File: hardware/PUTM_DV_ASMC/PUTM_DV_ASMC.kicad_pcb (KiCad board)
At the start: 4 copper layers, 80 x 60 mm, 172 parts, among them IC1 BTS722204ESAXUMA1, IC2 BTS722204ESAXUMA1, J1 FTSH-107-01-L-D-K, J2 IPBS-110-01-XX-D-GP, Q1 30V/5A, T1 TP_VCC, T2 TP_+5V, T3 TP_+3V3, T4 TP_GND, T5 TP_GND, T6 TP_VCC, T7 TP_GND, T8 TP_+5V, T9 TP_GND, U1 LM4040C33FTA, U2 STM32G484RETx, U3 LM1117-3.3, U4 TPS54202HDDCR, U5 ADM3057ExRW, U6 ADM3057ExRW, U8 TLP291-4, Y1 ATX-11-F-32.000MHZ-F05-T

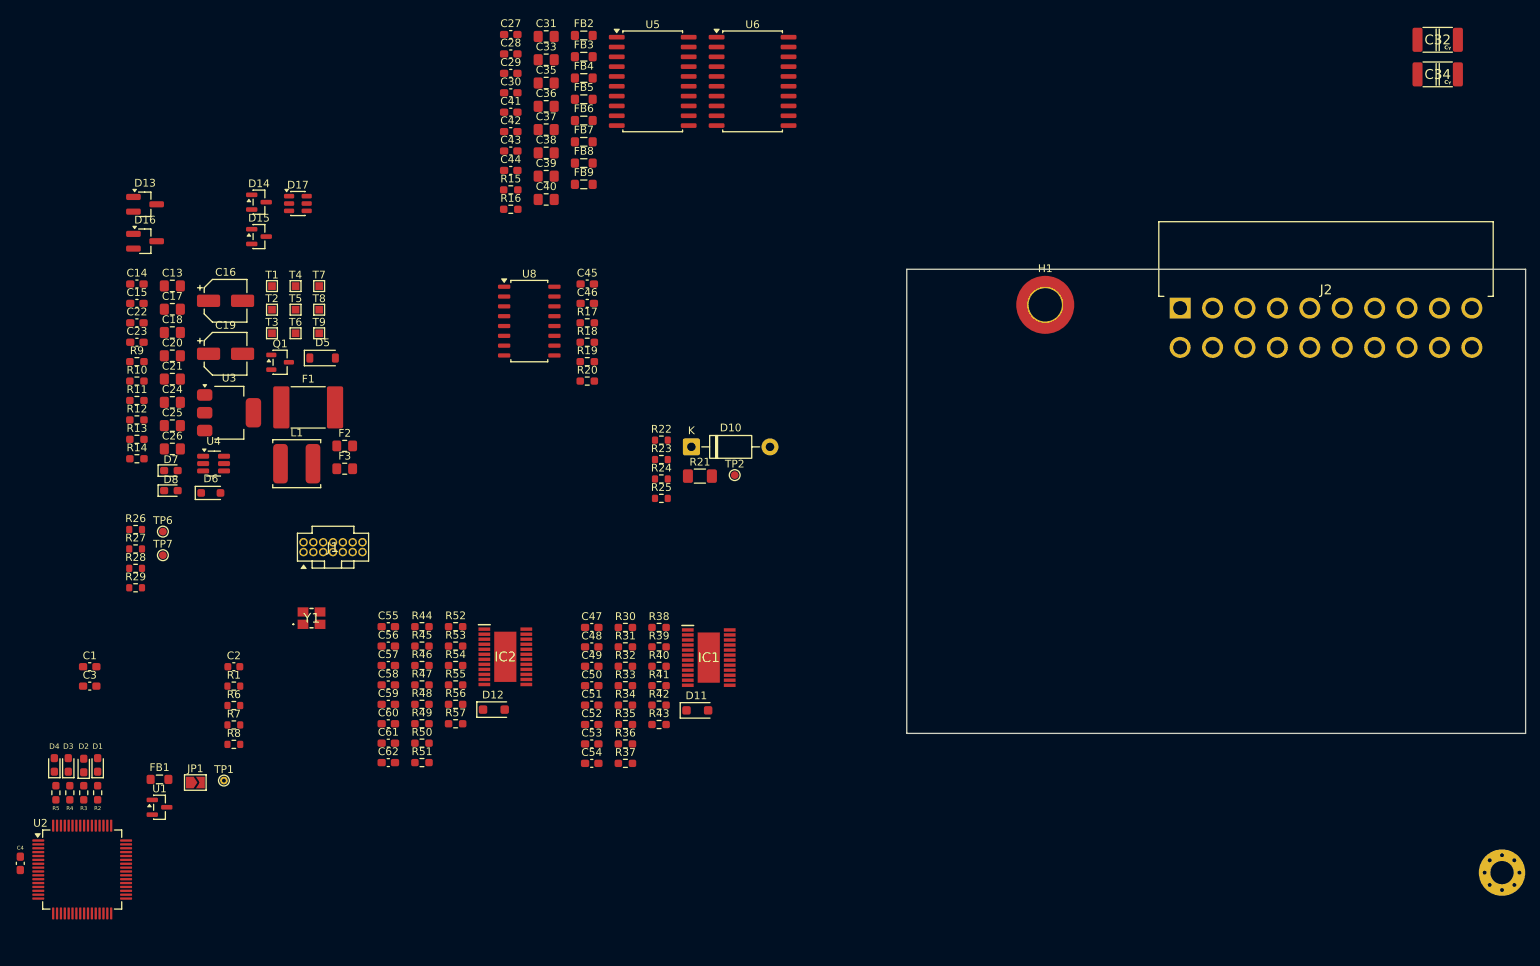
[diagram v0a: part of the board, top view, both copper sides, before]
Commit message: tylko dwa bledy z can - schemat na wykonczeniu
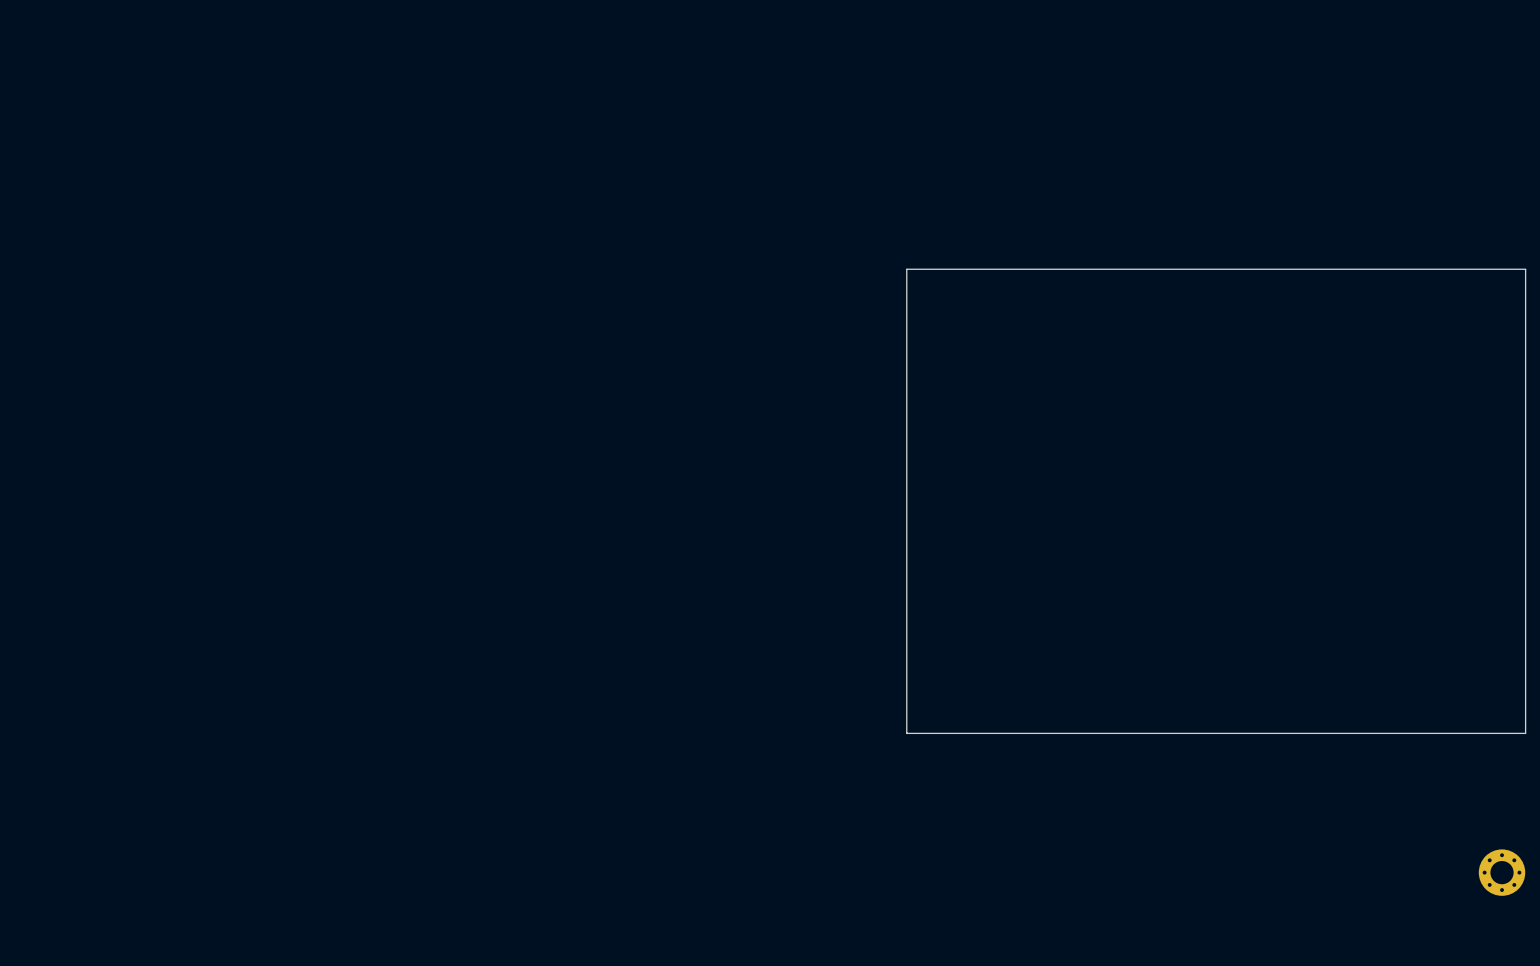
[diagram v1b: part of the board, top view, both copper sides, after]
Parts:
- removed C1, C3: 100nF, Capacitor_SMD:C_0603_1608Metric_Pad1.08x0.95mm_HandSolder
- removed C13, C18, C20: 10u, Capacitor_SMD:C_0805_2012Metric_Pad1.18x1.45mm_HandSolder
- removed C14, C15, C22, C23, C27, C28, C41, C43, C45, C46, C48, C56: 100n, Capacitor_SMD:C_0603_1608Metric_Pad1.08x0.95mm_HandSolder
- removed C16, C19: 22u, Capacitor_SMD:CP_Elec_5x5.8
- removed C17, C21, C24, C25, C26: 22u, Capacitor_SMD:C_0805_2012Metric_Pad1.18x1.45mm_HandSolder
- removed C2: 100n, Capacitor_SMD:C_0603_1608Metric
- removed C29, C30, C42, C44, C51, C52, C53, C54, C59, C60, C61, C62: 10n, Capacitor_SMD:C_0603_1608Metric_Pad1.08x0.95mm_HandSolder
- removed C31, C33, C35, C36, C37, C38, C39, C40: 47u, Capacitor_SMD:C_0805_2012Metric_Pad1.18x1.45mm_HandSolder
- removed C32, C34: 4.7nF/Y2, CAPC5728X280N:CAPC5728X280N
- removed C4: 6p, Capacitor_SMD:C_0603_1608Metric_Pad1.08x0.95mm_HandSolder
- removed C47, C55: 220p, Capacitor_SMD:C_0603_1608Metric_Pad1.08x0.95mm_HandSolder
- removed C49, C57: 22n, Capacitor_SMD:C_0603_1608Metric_Pad1.08x0.95mm_HandSolder
- removed C50, C58: 470n, Capacitor_SMD:C_0603_1608Metric_Pad1.08x0.95mm_HandSolder
- removed D1, D2, D3, D4: LED, LED_SMD:LED_0603_1608Metric_Pad1.05x0.95mm_HandSolder
- removed D10: 1N4007, Diode_THT:D_DO-41_SOD81_P10.16mm_Horizontal
- removed D11, D12: 40V/3A, Diode_SMD:D_SOD-123F
- removed D13, D16: PESD5V0L2BT, Package_TO_SOT_SMD:SOT-23_Handsoldering
- removed D14: BZX84C5V6, Package_TO_SOT_SMD:SOT-23
- removed D15: BZX84C3V6-E3-08, Package_TO_SOT_SMD:SOT-23
- removed D17: 3.6V/400W, Package_TO_SOT_SMD:SOT-23-6
- removed D5: 30V/200W, Diode_SMD:D_SOD-123
- removed D6: 9V1/200mW, Diode_SMD:D_SOD-323_HandSoldering
- removed D7: LED_+3V3, LED_SMD:LED_0603_1608Metric_Pad1.05x0.95mm_HandSolder
- removed D8: LED_+5V, LED_SMD:LED_0603_1608Metric_Pad1.05x0.95mm_HandSolder
- removed F1: 33V/1A5, Fuse:Fuse_2920_7451Metric_Pad2.10x5.45mm_HandSolder
- removed F2, F3: 6V/1A, Fuse:Fuse_0805_2012Metric_Pad1.15x1.40mm_HandSolder
- removed FB1, FB2, FB3, FB4, FB5, FB6, FB7, FB8, FB9: 2K@100MHz, Inductor_SMD:L_0805_2012Metric_Pad1.05x1.20mm_HandSolder
- removed H1: MountingHole_Pad_MP, MountingHole:MountingHole_4.3mm_M4_DIN965_Pad_TopOnly
- removed IC1, IC2: BTS722204ESAXUMA1, PDM:SOP65P600X115-25N
- removed J1: FTSH-107-01-L-D-K, FTSH-107-XX-YYY-D-K:FTSH-107-XX-YYY-D-K
- removed J2: IPBS-110-01-XX-D-GP, PDM:IPBT110H1TDRAGP
- removed JP1: Jumper_2_Small_Bridged, Jumper:SolderJumper-2_P1.3mm_Open_TrianglePad1.0x1.5mm
- removed L1: 68u/1A4, Inductor_SMD:L_TDK_VLS6045EX_VLS6045AF
- removed Q1: 30V/5A, Package_TO_SOT_SMD:SOT-23-3
- removed R1: 1k, Resistor_SMD:R_0603_1608Metric
- removed R10, R14: 1k, Resistor_SMD:R_0603_1608Metric_Pad0.98x0.95mm_HandSolder
- removed R11: 510k, Resistor_SMD:R_0603_1608Metric_Pad0.98x0.95mm_HandSolder
- removed R12: 13k3, Resistor_SMD:R_0603_1608Metric_Pad0.98x0.95mm_HandSolder
- removed R13, R9: 100k, Resistor_SMD:R_0603_1608Metric_Pad0.98x0.95mm_HandSolder
- removed R15, R16: 100K, Resistor_SMD:R_0603_1608Metric_Pad0.98x0.95mm_HandSolder
- removed R17, R18: 2k, Resistor_SMD:R_0603_1608Metric_Pad0.98x0.95mm_HandSolder
- removed R19, R20, R38, R39, R40, R41, R52, R53, R54, R55: 10k, Resistor_SMD:R_0603_1608Metric_Pad0.98x0.95mm_HandSolder
- removed R2, R3, R4, R5: 1K, Resistor_SMD:R_0603_1608Metric_Pad0.98x0.95mm_HandSolder
- removed R21: 2.2k, Resistor_SMD:R_1206_3216Metric_Pad1.30x1.75mm_HandSolder
- removed R22, R23, R26, R28: 100R, Resistor_SMD:R_0603_1608Metric
- removed R24, R25, R27, R29, R6, R7, R8: 10k, Resistor_SMD:R_0603_1608Metric
- removed R30, R31, R32, R44, R45, R46: 4k7, Resistor_SMD:R_0603_1608Metric_Pad0.98x0.95mm_HandSolder
- removed R33, R47: 470R, Resistor_SMD:R_0603_1608Metric_Pad0.98x0.95mm_HandSolder
- removed R34, R35, R36, R37, R48, R49, R50, R51: 330R, Resistor_SMD:R_0603_1608Metric_Pad0.98x0.95mm_HandSolder
- removed R42, R56: 1k2, Resistor_SMD:R_0603_1608Metric_Pad0.98x0.95mm_HandSolder
- removed R43, R57: 47R, Resistor_SMD:R_0603_1608Metric_Pad0.98x0.95mm_HandSolder
- removed T1, T6: TP_VCC, TestPoint:TestPoint_Pad_1.0x1.0mm
- removed T2, T8: TP_+5V, TestPoint:TestPoint_Pad_1.0x1.0mm
- removed T3: TP_+3V3, TestPoint:TestPoint_Pad_1.0x1.0mm
- removed T4, T5, T7, T9: TP_GND, TestPoint:TestPoint_Pad_1.0x1.0mm
- removed TP1: TestPoint_Small, TestPoint:TestPoint_THTPad_D1.0mm_Drill0.5mm
- removed TP2, TP6, TP7: TestPoint_Small, TestPoint:TestPoint_Pad_D1.0mm
- removed U1: LM4040C33FTA, Package_TO_SOT_SMD:SOT-23
- removed U2: STM32G484RETx, Package_QFP:LQFP-64_10x10mm_P0.5mm
- removed U3: LM1117-3.3, Package_TO_SOT_SMD:SOT-223-3_TabPin2
- removed U4: TPS54202HDDCR, Package_TO_SOT_SMD:SOT-23-6_Handsoldering
- removed U5, U6: ADM3057ExRW, Package_SO:SOIC-20W_7.5x12.8mm_P1.27mm
- removed U8: TLP291-4, Package_SO:SOIC-16_4.55x10.3mm_P1.27mm
- removed Y1: ATX-11-F-32.000MHZ-F05-T, ATX11F32000MHZF05T:ATX11F32000MHZF05T

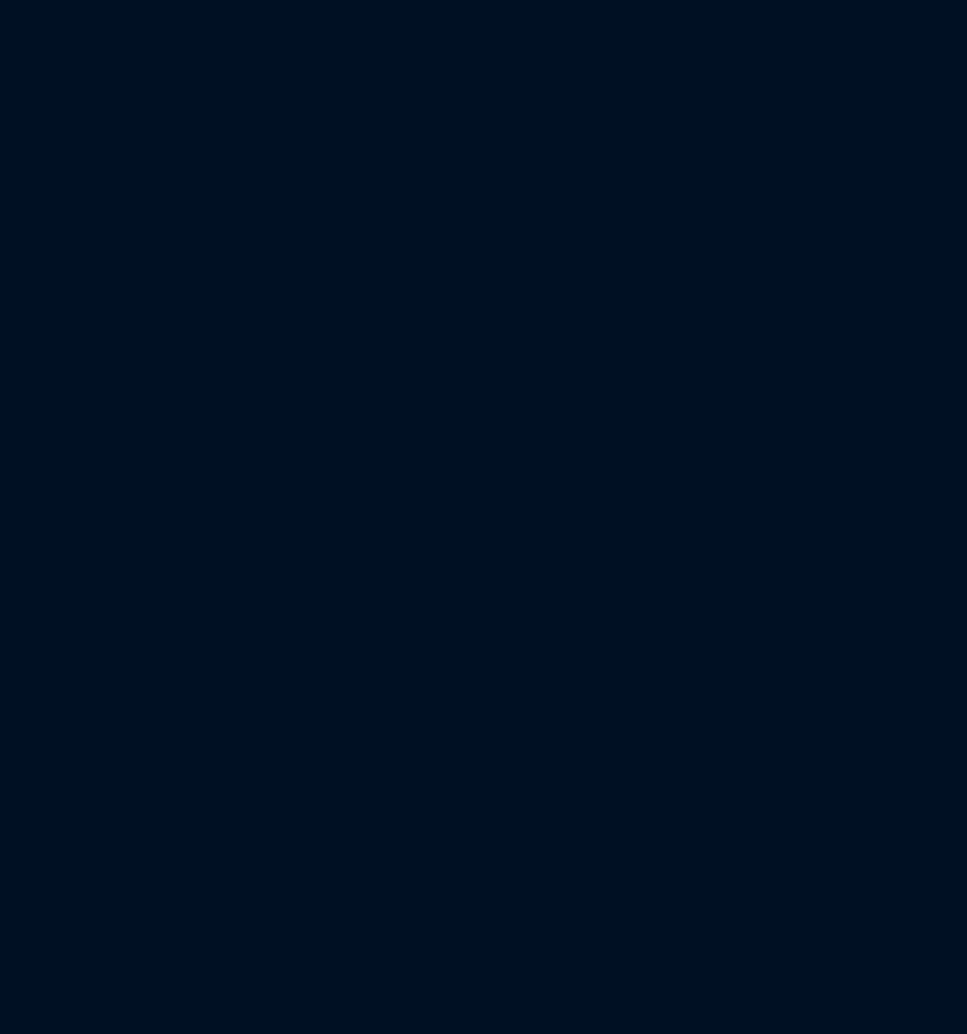
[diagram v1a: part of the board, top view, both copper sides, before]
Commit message: poprawki footprint
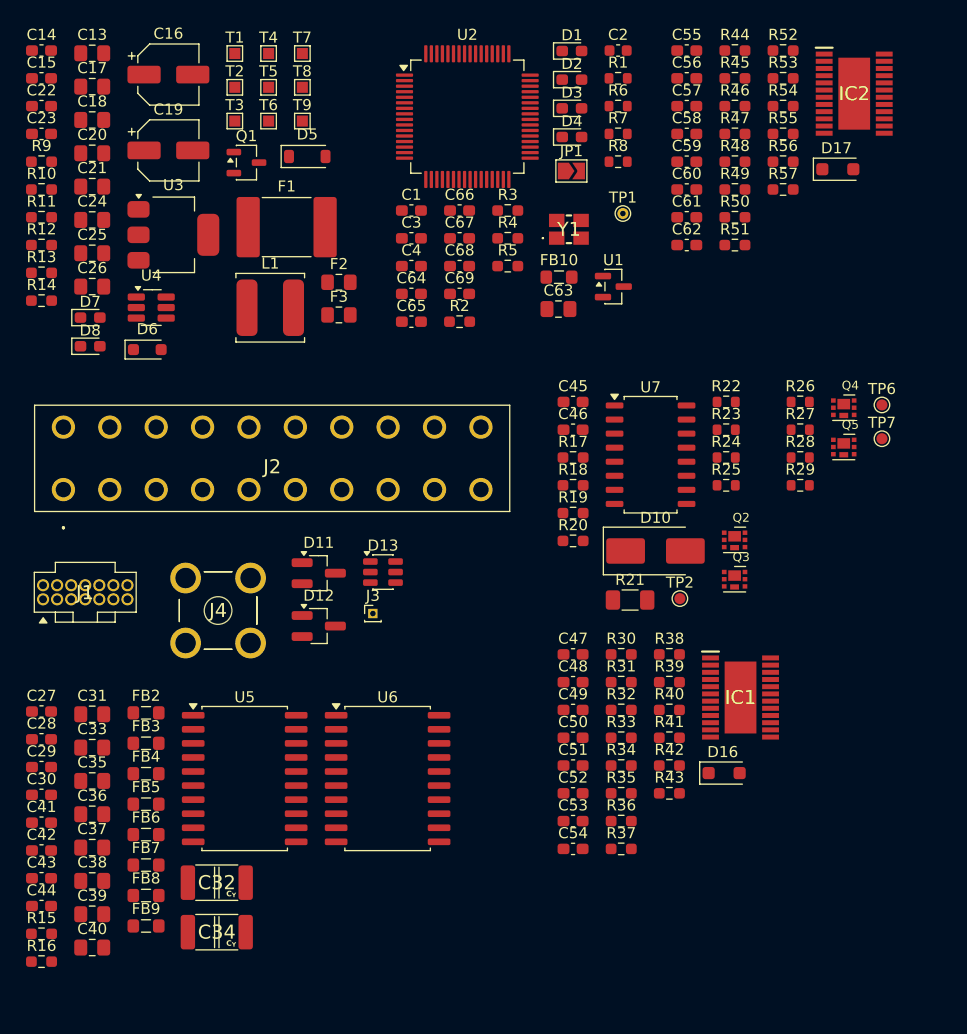
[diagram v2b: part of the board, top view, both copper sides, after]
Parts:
- added C1: 100nF, Capacitor_SMD:C_0603_1608Metric_Pad1.08x0.95mm_HandSolder, F.Cu at (27.1, 17.6)
- added C13: 10u, Capacitor_SMD:C_0805_2012Metric_Pad1.18x1.45mm_HandSolder, F.Cu at (-1.75, 3.40)
- added C14: 100n, Capacitor_SMD:C_0603_1608Metric_Pad1.08x0.95mm_HandSolder, F.Cu at (-6.33, 3.15)
- added C15: 100n, Capacitor_SMD:C_0603_1608Metric_Pad1.08x0.95mm_HandSolder, F.Cu at (-6.33, 5.67)
- added C16: 22u, Capacitor_SMD:CP_Elec_5x5.8, F.Cu at (5.13, 5.33)
- added C17: 22u, Capacitor_SMD:C_0805_2012Metric_Pad1.18x1.45mm_HandSolder, F.Cu at (-1.75, 6.42)
- added C18: 10u, Capacitor_SMD:C_0805_2012Metric_Pad1.18x1.45mm_HandSolder, F.Cu at (-1.75, 9.43)
- added C19: 22u, Capacitor_SMD:CP_Elec_5x5.8, F.Cu at (5.13, 12.2)
- added C2: 100n, Capacitor_SMD:C_0603_1608Metric, F.Cu at (45.8, 3.15)
- added C20: 10u, Capacitor_SMD:C_0805_2012Metric_Pad1.18x1.45mm_HandSolder, F.Cu at (-1.75, 12.4)
- added C21: 22u, Capacitor_SMD:C_0805_2012Metric_Pad1.18x1.45mm_HandSolder, F.Cu at (-1.75, 15.4)
- added C22: 100n, Capacitor_SMD:C_0603_1608Metric_Pad1.08x0.95mm_HandSolder, F.Cu at (-6.33, 8.18)
- added C23: 100n, Capacitor_SMD:C_0603_1608Metric_Pad1.08x0.95mm_HandSolder, F.Cu at (-6.33, 10.7)
- added C24: 22u, Capacitor_SMD:C_0805_2012Metric_Pad1.18x1.45mm_HandSolder, F.Cu at (-1.75, 18.5)
- added C25: 22u, Capacitor_SMD:C_0805_2012Metric_Pad1.18x1.45mm_HandSolder, F.Cu at (-1.75, 21.5)
- added C26: 22u, Capacitor_SMD:C_0805_2012Metric_Pad1.18x1.45mm_HandSolder, F.Cu at (-1.75, 24.5)
- added C27: 100n, Capacitor_SMD:C_0603_1608Metric_Pad1.08x0.95mm_HandSolder, F.Cu at (-6.33, 62.9)
- added C28: 100n, Capacitor_SMD:C_0603_1608Metric_Pad1.08x0.95mm_HandSolder, F.Cu at (-6.33, 65.4)
- added C29: 10n, Capacitor_SMD:C_0603_1608Metric_Pad1.08x0.95mm_HandSolder, F.Cu at (-6.33, 67.9)
- added C3: 100nF, Capacitor_SMD:C_0603_1608Metric_Pad1.08x0.95mm_HandSolder, F.Cu at (27.1, 20.1)
- added C30: 10n, Capacitor_SMD:C_0603_1608Metric_Pad1.08x0.95mm_HandSolder, F.Cu at (-6.33, 70.4)
- added C31: 47u, Capacitor_SMD:C_0805_2012Metric_Pad1.18x1.45mm_HandSolder, F.Cu at (-1.75, 63.1)
- added C32: 4.7nF/Y2, CAPC5728X280N:CAPC5728X280N, F.Cu at (9.51, 78.3)
- added C33: 47u, Capacitor_SMD:C_0805_2012Metric_Pad1.18x1.45mm_HandSolder, F.Cu at (-1.75, 66.1)
- added C34: 4.7nF/Y2, CAPC5728X280N:CAPC5728X280N, F.Cu at (9.51, 82.8)
- added C35: 47u, Capacitor_SMD:C_0805_2012Metric_Pad1.18x1.45mm_HandSolder, F.Cu at (-1.75, 69.1)
- added C36: 47u, Capacitor_SMD:C_0805_2012Metric_Pad1.18x1.45mm_HandSolder, F.Cu at (-1.75, 72.1)
- added C37: 47u, Capacitor_SMD:C_0805_2012Metric_Pad1.18x1.45mm_HandSolder, F.Cu at (-1.75, 75.1)
- added C38: 47u, Capacitor_SMD:C_0805_2012Metric_Pad1.18x1.45mm_HandSolder, F.Cu at (-1.75, 78.2)
- added C39: 47u, Capacitor_SMD:C_0805_2012Metric_Pad1.18x1.45mm_HandSolder, F.Cu at (-1.75, 81.2)
- added C4: 6p, Capacitor_SMD:C_0603_1608Metric_Pad1.08x0.95mm_HandSolder, F.Cu at (27.1, 22.6)
- added C40: 47u, Capacitor_SMD:C_0805_2012Metric_Pad1.18x1.45mm_HandSolder, F.Cu at (-1.75, 84.2)
- added C41: 100n, Capacitor_SMD:C_0603_1608Metric_Pad1.08x0.95mm_HandSolder, F.Cu at (-6.33, 72.9)
- added C42: 10n, Capacitor_SMD:C_0603_1608Metric_Pad1.08x0.95mm_HandSolder, F.Cu at (-6.33, 75.4)
- added C43: 100n, Capacitor_SMD:C_0603_1608Metric_Pad1.08x0.95mm_HandSolder, F.Cu at (-6.33, 77.9)
- added C44: 10n, Capacitor_SMD:C_0603_1608Metric_Pad1.08x0.95mm_HandSolder, F.Cu at (-6.33, 80.4)
- added C45: 100n, Capacitor_SMD:C_0603_1608Metric_Pad1.08x0.95mm_HandSolder, F.Cu at (41.7, 34.9)
- added C46: 100n, Capacitor_SMD:C_0603_1608Metric_Pad1.08x0.95mm_HandSolder, F.Cu at (41.7, 37.4)
- added C47: 220p, Capacitor_SMD:C_0603_1608Metric_Pad1.08x0.95mm_HandSolder, F.Cu at (41.7, 57.7)
- added C48: 100n, Capacitor_SMD:C_0603_1608Metric_Pad1.08x0.95mm_HandSolder, F.Cu at (41.7, 60.2)
- added C49: 22n, Capacitor_SMD:C_0603_1608Metric_Pad1.08x0.95mm_HandSolder, F.Cu at (41.7, 62.7)
- added C50: 470n, Capacitor_SMD:C_0603_1608Metric_Pad1.08x0.95mm_HandSolder, F.Cu at (41.7, 65.2)
- added C51: 10n, Capacitor_SMD:C_0603_1608Metric_Pad1.08x0.95mm_HandSolder, F.Cu at (41.7, 67.7)
- added C52: 10n, Capacitor_SMD:C_0603_1608Metric_Pad1.08x0.95mm_HandSolder, F.Cu at (41.7, 70.2)
- added C53: 10n, Capacitor_SMD:C_0603_1608Metric_Pad1.08x0.95mm_HandSolder, F.Cu at (41.7, 72.8)
- added C54: 10n, Capacitor_SMD:C_0603_1608Metric_Pad1.08x0.95mm_HandSolder, F.Cu at (41.7, 75.3)
- added C55: 220p, Capacitor_SMD:C_0603_1608Metric_Pad1.08x0.95mm_HandSolder, F.Cu at (52.0, 3.15)
- added C56: 100n, Capacitor_SMD:C_0603_1608Metric_Pad1.08x0.95mm_HandSolder, F.Cu at (52.0, 5.67)
- added C57: 22n, Capacitor_SMD:C_0603_1608Metric_Pad1.08x0.95mm_HandSolder, F.Cu at (52.0, 8.18)
- added C58: 470n, Capacitor_SMD:C_0603_1608Metric_Pad1.08x0.95mm_HandSolder, F.Cu at (52.0, 10.7)
- added C59: 10n, Capacitor_SMD:C_0603_1608Metric_Pad1.08x0.95mm_HandSolder, F.Cu at (52.0, 13.2)
- added C60: 10n, Capacitor_SMD:C_0603_1608Metric_Pad1.08x0.95mm_HandSolder, F.Cu at (52.0, 15.7)
- added C61: 10n, Capacitor_SMD:C_0603_1608Metric_Pad1.08x0.95mm_HandSolder, F.Cu at (52.0, 18.2)
- added C62: 10n, Capacitor_SMD:C_0603_1608Metric_Pad1.08x0.95mm_HandSolder, F.Cu at (52.0, 20.7)
- added C63: 10u, Capacitor_SMD:C_0805_2012Metric_Pad1.18x1.45mm_HandSolder, F.Cu at (40.4, 26.5)
- added C64: 100nF, Capacitor_SMD:C_0603_1608Metric_Pad1.08x0.95mm_HandSolder, F.Cu at (27.1, 25.1)
- added C65: 100nF, Capacitor_SMD:C_0603_1608Metric_Pad1.08x0.95mm_HandSolder, F.Cu at (27.1, 27.6)
- added C66: 100nF, Capacitor_SMD:C_0603_1608Metric_Pad1.08x0.95mm_HandSolder, F.Cu at (31.4, 17.6)
- added C67: 100nF, Capacitor_SMD:C_0603_1608Metric_Pad1.08x0.95mm_HandSolder, F.Cu at (31.4, 20.1)
- added C68: 100nF, Capacitor_SMD:C_0603_1608Metric_Pad1.08x0.95mm_HandSolder, F.Cu at (31.4, 22.6)
- added C69: 100nF, Capacitor_SMD:C_0603_1608Metric_Pad1.08x0.95mm_HandSolder, F.Cu at (31.4, 25.1)
- added D1: LED, LED_SMD:LED_0603_1608Metric_Pad1.05x0.95mm_HandSolder, F.Cu at (41.6, 3.19)
- added D10: SMBJ30A, Diode_SMD:D_SMB_Handsoldering, F.Cu at (49.1, 48.4)
- added D11: PESD5V0L2BT, Package_TO_SOT_SMD:SOT-23_Handsoldering, F.Cu at (18.7, 50.4)
- added D12: PESD5V0L2BT, Package_TO_SOT_SMD:SOT-23_Handsoldering, F.Cu at (18.7, 55.1)
- added D13: 3.6V/400W, Package_TO_SOT_SMD:SOT-23-6, F.Cu at (24.5, 50.3)
- added D16: 40V/3A, Diode_SMD:D_SOD-123F, F.Cu at (55.3, 68.4)
- added D17: 40V/3A, Diode_SMD:D_SOD-123F, F.Cu at (65.6, 13.9)
- added D2: LED, LED_SMD:LED_0603_1608Metric_Pad1.05x0.95mm_HandSolder, F.Cu at (41.6, 5.79)
- added D3: LED, LED_SMD:LED_0603_1608Metric_Pad1.05x0.95mm_HandSolder, F.Cu at (41.6, 8.38)
- added D4: LED, LED_SMD:LED_0603_1608Metric_Pad1.05x0.95mm_HandSolder, F.Cu at (41.6, 11.0)
- added D5: 30V/200W, Diode_SMD:D_SOD-123, F.Cu at (17.7, 12.7)
- added D6: 9V1/200mW, Diode_SMD:D_SOD-323_HandSoldering, F.Cu at (3.23, 30.2)
- added D7: LED_+3V3, LED_SMD:LED_0603_1608Metric_Pad1.05x0.95mm_HandSolder, F.Cu at (-1.93, 27.3)
- added D8: LED_+5V, LED_SMD:LED_0603_1608Metric_Pad1.05x0.95mm_HandSolder, F.Cu at (-1.93, 29.9)
- added F1: 33V/1A5, Fuse:Fuse_2920_7451Metric_Pad2.10x5.45mm_HandSolder, F.Cu at (15.8, 19.1)
- added F2: 6V/1A, Fuse:Fuse_0805_2012Metric_Pad1.15x1.40mm_HandSolder, F.Cu at (20.5, 24.1)
- added F3: 6V/1A, Fuse:Fuse_0805_2012Metric_Pad1.15x1.40mm_HandSolder, F.Cu at (20.5, 27.0)
- added FB10: 2K@100MHz, Inductor_SMD:L_0805_2012Metric_Pad1.05x1.20mm_HandSolder, F.Cu at (40.4, 23.6)
- added FB2: 2K@100MHz, Inductor_SMD:L_0805_2012Metric_Pad1.05x1.20mm_HandSolder, F.Cu at (3.12, 63.0)
- added FB3: 2K@100MHz, Inductor_SMD:L_0805_2012Metric_Pad1.05x1.20mm_HandSolder, F.Cu at (3.12, 65.7)
- added FB4: 2K@100MHz, Inductor_SMD:L_0805_2012Metric_Pad1.05x1.20mm_HandSolder, F.Cu at (3.12, 68.5)
- added FB5: 2K@100MHz, Inductor_SMD:L_0805_2012Metric_Pad1.05x1.20mm_HandSolder, F.Cu at (3.12, 71.2)
- added FB6: 2K@100MHz, Inductor_SMD:L_0805_2012Metric_Pad1.05x1.20mm_HandSolder, F.Cu at (3.12, 74.0)
- added FB7: 2K@100MHz, Inductor_SMD:L_0805_2012Metric_Pad1.05x1.20mm_HandSolder, F.Cu at (3.12, 76.7)
- added FB8: 2K@100MHz, Inductor_SMD:L_0805_2012Metric_Pad1.05x1.20mm_HandSolder, F.Cu at (3.12, 79.5)
- added FB9: 2K@100MHz, Inductor_SMD:L_0805_2012Metric_Pad1.05x1.20mm_HandSolder, F.Cu at (3.12, 82.2)
- added IC1: BTS722204ESAXUMA1, BTS722204ESAXUMA1:SOP65P600X115-25N, F.Cu at (56.8, 61.6)
- added IC2: BTS722204ESAXUMA1, BTS722204ESAXUMA1:SOP65P600X115-25N, F.Cu at (67.1, 7.05)
- added J1: FTSH-107-01-L-D-K, FTSH-107-XX-YYY-D-K:FTSH-107-XX-YYY-D-K, F.Cu at (-2.38, 52.1)
- added J2: IPBS-110-01-XX-D-GP, IPBS-110-01-T-D-GP:IPBS11001TDGP, F.Cu at (-4.35, 42.8)
- added J3: Conn_01x01_Socket, Connector_PinHeader_1.00mm:PinHeader_1x01_P1.00mm_Vertical, F.Cu at (23.6, 54.0)
- added J4: 74650073R, 74650073R:74650073R, F.Cu at (6.69, 56.7)
- added JP1: Jumper_2_Small_Bridged, Jumper:SolderJumper-2_P1.3mm_Open_TrianglePad1.0x1.5mm, F.Cu at (41.5, 14.0)
- added L1: 68u/1A4, Inductor_SMD:L_TDK_VLS6045EX_VLS6045AF, F.Cu at (14.3, 26.4)
- added Q1: 30V/5A, Package_TO_SOT_SMD:SOT-23-3, F.Cu at (12.2, 13.3)
- added Q2: BUK6D210, UDFN2020-6:Diodes_UDFN2020-6_Type-F, F.Cu at (56.3, 47.4)
- added Q3: BUK6D210, UDFN2020-6:Diodes_UDFN2020-6_Type-F, F.Cu at (56.3, 50.9)
- added Q4: BUK6D210, UDFN2020-6:Diodes_UDFN2020-6_Type-F, F.Cu at (66.1, 35.4)
- added Q5: BUK6D210, UDFN2020-6:Diodes_UDFN2020-6_Type-F, F.Cu at (66.1, 39.0)
- added R1: 1k, Resistor_SMD:R_0603_1608Metric, F.Cu at (45.8, 5.67)
- added R10: 1k, Resistor_SMD:R_0603_1608Metric_Pad0.98x0.95mm_HandSolder, F.Cu at (-6.33, 15.7)
- added R11: 510k, Resistor_SMD:R_0603_1608Metric_Pad0.98x0.95mm_HandSolder, F.Cu at (-6.33, 18.2)
- added R12: 13k3, Resistor_SMD:R_0603_1608Metric_Pad0.98x0.95mm_HandSolder, F.Cu at (-6.33, 20.7)
- added R13: 100k, Resistor_SMD:R_0603_1608Metric_Pad0.98x0.95mm_HandSolder, F.Cu at (-6.33, 23.2)
- added R14: 1k, Resistor_SMD:R_0603_1608Metric_Pad0.98x0.95mm_HandSolder, F.Cu at (-6.33, 25.7)
- added R15: 100K, Resistor_SMD:R_0603_1608Metric_Pad0.98x0.95mm_HandSolder, F.Cu at (-6.33, 82.9)
- added R16: 100K, Resistor_SMD:R_0603_1608Metric_Pad0.98x0.95mm_HandSolder, F.Cu at (-6.33, 85.4)
- added R17: 2k, Resistor_SMD:R_0603_1608Metric_Pad0.98x0.95mm_HandSolder, F.Cu at (41.7, 39.9)
- added R18: 2k, Resistor_SMD:R_0603_1608Metric_Pad0.98x0.95mm_HandSolder, F.Cu at (41.7, 42.4)
- added R19: 10k, Resistor_SMD:R_0603_1608Metric_Pad0.98x0.95mm_HandSolder, F.Cu at (41.7, 44.9)
- added R2: 1K, Resistor_SMD:R_0603_1608Metric_Pad0.98x0.95mm_HandSolder, F.Cu at (31.4, 27.6)
- added R20: 10k, Resistor_SMD:R_0603_1608Metric_Pad0.98x0.95mm_HandSolder, F.Cu at (41.7, 47.4)
- added R21: 2.2k, Resistor_SMD:R_1206_3216Metric_Pad1.30x1.75mm_HandSolder, F.Cu at (46.8, 52.8)
- added R22: 100R, Resistor_SMD:R_0603_1608Metric, F.Cu at (55.5, 34.9)
- added R23: 100R, Resistor_SMD:R_0603_1608Metric, F.Cu at (55.5, 37.4)
- added R24: 10k, Resistor_SMD:R_0603_1608Metric, F.Cu at (55.5, 39.9)
- added R25: 10k, Resistor_SMD:R_0603_1608Metric, F.Cu at (55.5, 42.4)
- added R26: 100R, Resistor_SMD:R_0603_1608Metric, F.Cu at (62.2, 34.9)
- added R27: 10k, Resistor_SMD:R_0603_1608Metric, F.Cu at (62.2, 37.4)
- added R28: 100R, Resistor_SMD:R_0603_1608Metric, F.Cu at (62.2, 39.9)
- added R29: 10k, Resistor_SMD:R_0603_1608Metric, F.Cu at (62.2, 42.4)
- added R3: 1K, Resistor_SMD:R_0603_1608Metric_Pad0.98x0.95mm_HandSolder, F.Cu at (35.8, 17.6)
- added R30: 4k7, Resistor_SMD:R_0603_1608Metric_Pad0.98x0.95mm_HandSolder, F.Cu at (46.0, 57.7)
- added R31: 4k7, Resistor_SMD:R_0603_1608Metric_Pad0.98x0.95mm_HandSolder, F.Cu at (46.0, 60.2)
- added R32: 4k7, Resistor_SMD:R_0603_1608Metric_Pad0.98x0.95mm_HandSolder, F.Cu at (46.0, 62.7)
- added R33: 470R, Resistor_SMD:R_0603_1608Metric_Pad0.98x0.95mm_HandSolder, F.Cu at (46.0, 65.2)
- added R34: 330R, Resistor_SMD:R_0603_1608Metric_Pad0.98x0.95mm_HandSolder, F.Cu at (46.0, 67.7)
- added R35: 330R, Resistor_SMD:R_0603_1608Metric_Pad0.98x0.95mm_HandSolder, F.Cu at (46.0, 70.2)
- added R36: 330R, Resistor_SMD:R_0603_1608Metric_Pad0.98x0.95mm_HandSolder, F.Cu at (46.0, 72.8)
- added R37: 330R, Resistor_SMD:R_0603_1608Metric_Pad0.98x0.95mm_HandSolder, F.Cu at (46.0, 75.3)
- added R38: 10k, Resistor_SMD:R_0603_1608Metric_Pad0.98x0.95mm_HandSolder, F.Cu at (50.4, 57.7)
- added R39: 10k, Resistor_SMD:R_0603_1608Metric_Pad0.98x0.95mm_HandSolder, F.Cu at (50.4, 60.2)
- added R4: 1K, Resistor_SMD:R_0603_1608Metric_Pad0.98x0.95mm_HandSolder, F.Cu at (35.8, 20.1)
- added R40: 10k, Resistor_SMD:R_0603_1608Metric_Pad0.98x0.95mm_HandSolder, F.Cu at (50.4, 62.7)
- added R41: 10k, Resistor_SMD:R_0603_1608Metric_Pad0.98x0.95mm_HandSolder, F.Cu at (50.4, 65.2)
- added R42: 1k2, Resistor_SMD:R_0603_1608Metric_Pad0.98x0.95mm_HandSolder, F.Cu at (50.4, 67.7)
- added R43: 47R, Resistor_SMD:R_0603_1608Metric_Pad0.98x0.95mm_HandSolder, F.Cu at (50.4, 70.2)
- added R44: 4k7, Resistor_SMD:R_0603_1608Metric_Pad0.98x0.95mm_HandSolder, F.Cu at (56.3, 3.15)
- added R45: 4k7, Resistor_SMD:R_0603_1608Metric_Pad0.98x0.95mm_HandSolder, F.Cu at (56.3, 5.67)
- added R46: 4k7, Resistor_SMD:R_0603_1608Metric_Pad0.98x0.95mm_HandSolder, F.Cu at (56.3, 8.18)
- added R47: 470R, Resistor_SMD:R_0603_1608Metric_Pad0.98x0.95mm_HandSolder, F.Cu at (56.3, 10.7)
- added R48: 330R, Resistor_SMD:R_0603_1608Metric_Pad0.98x0.95mm_HandSolder, F.Cu at (56.3, 13.2)
- added R49: 330R, Resistor_SMD:R_0603_1608Metric_Pad0.98x0.95mm_HandSolder, F.Cu at (56.3, 15.7)
- added R5: 1K, Resistor_SMD:R_0603_1608Metric_Pad0.98x0.95mm_HandSolder, F.Cu at (35.8, 22.6)
- added R50: 330R, Resistor_SMD:R_0603_1608Metric_Pad0.98x0.95mm_HandSolder, F.Cu at (56.3, 18.2)
- added R51: 330R, Resistor_SMD:R_0603_1608Metric_Pad0.98x0.95mm_HandSolder, F.Cu at (56.3, 20.7)
- added R52: 10k, Resistor_SMD:R_0603_1608Metric_Pad0.98x0.95mm_HandSolder, F.Cu at (60.7, 3.15)
- added R53: 10k, Resistor_SMD:R_0603_1608Metric_Pad0.98x0.95mm_HandSolder, F.Cu at (60.7, 5.67)
- added R54: 10k, Resistor_SMD:R_0603_1608Metric_Pad0.98x0.95mm_HandSolder, F.Cu at (60.7, 8.18)
- added R55: 10k, Resistor_SMD:R_0603_1608Metric_Pad0.98x0.95mm_HandSolder, F.Cu at (60.7, 10.7)
- added R56: 1k2, Resistor_SMD:R_0603_1608Metric_Pad0.98x0.95mm_HandSolder, F.Cu at (60.7, 13.2)
- added R57: 47R, Resistor_SMD:R_0603_1608Metric_Pad0.98x0.95mm_HandSolder, F.Cu at (60.7, 15.7)
- added R6: 10k, Resistor_SMD:R_0603_1608Metric, F.Cu at (45.8, 8.18)
- added R7: 10k, Resistor_SMD:R_0603_1608Metric, F.Cu at (45.8, 10.7)
- added R8: 10k, Resistor_SMD:R_0603_1608Metric, F.Cu at (45.8, 13.2)
- added R9: 100k, Resistor_SMD:R_0603_1608Metric_Pad0.98x0.95mm_HandSolder, F.Cu at (-6.33, 13.2)
- added T1: TP_VCC, TestPoint:TestPoint_Pad_1.0x1.0mm, F.Cu at (11.1, 3.42)
- added T2: TP_+5V, TestPoint:TestPoint_Pad_1.0x1.0mm, F.Cu at (11.1, 6.47)
- added T3: TP_+3V3, TestPoint:TestPoint_Pad_1.0x1.0mm, F.Cu at (11.1, 9.53)
- added T4: TP_GND, TestPoint:TestPoint_Pad_1.0x1.0mm, F.Cu at (14.2, 3.42)
- added T5: TP_GND, TestPoint:TestPoint_Pad_1.0x1.0mm, F.Cu at (14.2, 6.47)
- added T6: TP_VCC, TestPoint:TestPoint_Pad_1.0x1.0mm, F.Cu at (14.2, 9.53)
- added T7: TP_GND, TestPoint:TestPoint_Pad_1.0x1.0mm, F.Cu at (17.2, 3.42)
- added T8: TP_+5V, TestPoint:TestPoint_Pad_1.0x1.0mm, F.Cu at (17.2, 6.47)
- added T9: TP_GND, TestPoint:TestPoint_Pad_1.0x1.0mm, F.Cu at (17.2, 9.53)
- added TP1: TestPoint_Small, TestPoint:TestPoint_THTPad_D1.0mm_Drill0.5mm, F.Cu at (46.2, 17.9)
- added TP2: TestPoint_Small, TestPoint:TestPoint_Pad_D1.0mm, F.Cu at (51.3, 52.7)
- added TP6: TestPoint_Small, TestPoint:TestPoint_Pad_D1.0mm, F.Cu at (69.6, 35.2)
- added TP7: TestPoint_Small, TestPoint:TestPoint_Pad_D1.0mm, F.Cu at (69.6, 38.2)
- added U1: LM4040C33FTA, Package_TO_SOT_SMD:SOT-23, F.Cu at (45.3, 24.5)
- added U2: STM32G484RETx, Package_QFP:LQFP-64_10x10mm_P0.5mm, F.Cu at (32.1, 9.12)
- added U3: LM1117-3.3, Package_TO_SOT_SMD:SOT-223-3_TabPin2, F.Cu at (5.58, 19.8)
- added U4: TPS54202HDDCR, Package_TO_SOT_SMD:SOT-23-6_Handsoldering, F.Cu at (3.58, 26.4)
- added U5: ADM3057ExRW, Package_SO:SOIC-20W_7.5x12.8mm_P1.27mm, F.Cu at (12.0, 68.9)
- added U6: ADM3057ExRW, Package_SO:SOIC-20W_7.5x12.8mm_P1.27mm, F.Cu at (24.9, 68.9)
- added U7: TLP291-4, Package_SO:SOIC-16_4.55x10.3mm_P1.27mm, F.Cu at (48.7, 39.7)
- added Y1: ATX-11-F-32.000MHZ-F05-T, ATX11F32000MHZF05T:ATX11F32000MHZF05T, F.Cu at (41.3, 19.3)

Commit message: work on power layout
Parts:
- C51, C52, C53, C54, C59, C60, C61, C62: moved to B.Cu
- moved T2 284.3 mm to (290.8, 57.6)
- moved T3 284.3 mm to (290.8, 60.6)
- moved T4 281.0 mm to (291.0, 52.0)
- moved T6 266.3 mm to (275.2, 62.2)
- moved T7 264.2 mm to (275.6, 58.6)
- moved T8 243.4 mm to (257.7, 44.1)
- moved T9 243.4 mm to (257.7, 47.1)
- moved C14 239.2 mm to (211.2, 102.6)
- moved C13 235.9 mm to (211.2, 105.0)
- moved T1 227.1 mm to (238.0, 13.7)
- moved T5 227.1 mm to (241.1, 16.7)
- moved C15 226.3 mm to (195.7, 107.5), turned to -90 degrees
- moved C18 224.6 mm to (212.0, 78.4)
- moved C23 224.5 mm to (205.0, 86.4)
- moved C20 224.4 mm to (212.0, 80.6)
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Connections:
- J2 pad 1: /Connectors/CAN1+ -> GND
- J2 pad 11: /Connectors/CAN2+ -> /Connectors/OUT_LIDAR
- J2 pad 12: /Connectors/CAN2- -> /Connectors/OUT_LIDAR
- J2 pad 13: /Connectors/OUT_LIDAR -> /Connectors/OUT_ASSI
- J2 pad 14: /Connectors/OUT_LIDAR -> /Connectors/OUT_ASSI
- J2 pad 15: /Connectors/OUT_ASSI -> /Connectors/OUT_RES
- J2 pad 16: /Connectors/OUT_ASSI -> /Connectors/OUT_EBS
- J2 pad 17: /Connectors/OUT_EBS -> /Connectors/CAN2+
- J2 pad 18: /Connectors/OUT_RES -> /Connectors/CAN2-
- J2 pad 19: /Connectors/GPIO -> /Connectors/CAN1-
- J2 pad 2: /Connectors/CAN1- -> /Connectors/GPIO
- J2 pad 20: GND -> /Connectors/CAN1+
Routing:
- net /DV_power_supply/Odrive_power_supply/IN3: track 0.00 -> 0.66 mm
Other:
- board size 80 x 60 mm -> 100 x 60 mm
- board text added: "24V -> 5V"
- board text added: "5V->3V3"
- board text added: "RPP"
